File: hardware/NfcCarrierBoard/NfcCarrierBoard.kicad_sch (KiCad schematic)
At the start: 32 parts, among them J1 Barrel_Jack, J2 Conn_01x03, J3 JST SH 4, J4 Grove, J5 Conn_01x03, Q1 NMOS, Q2 NMOS, SW1 RESET

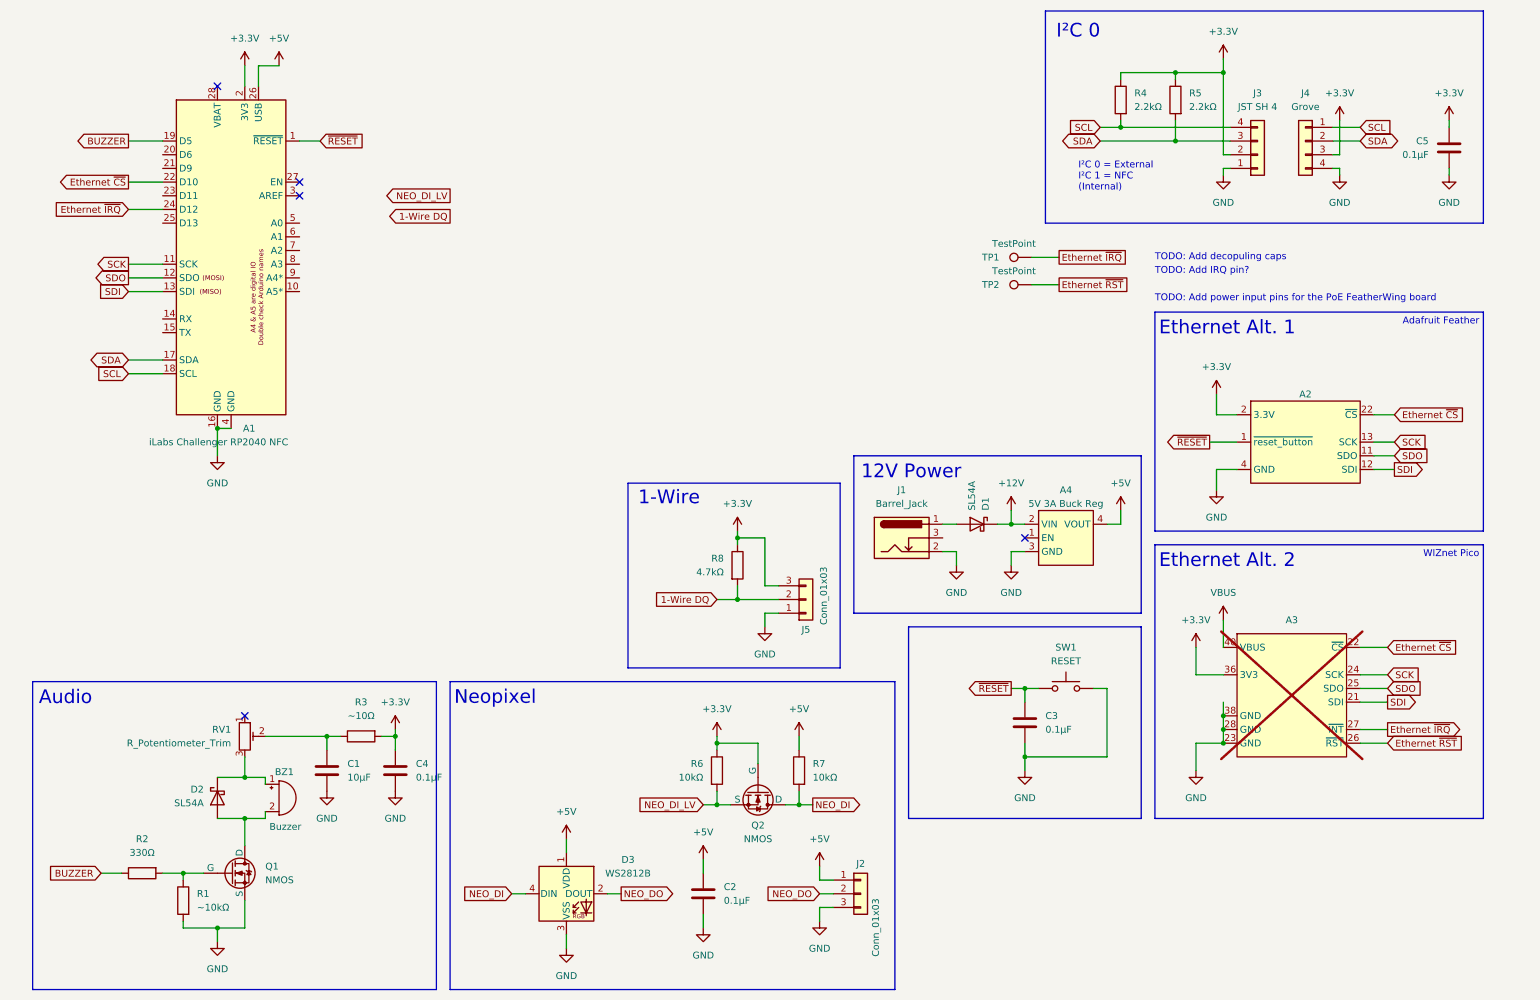
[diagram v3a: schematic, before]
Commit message: Add decopuling caps
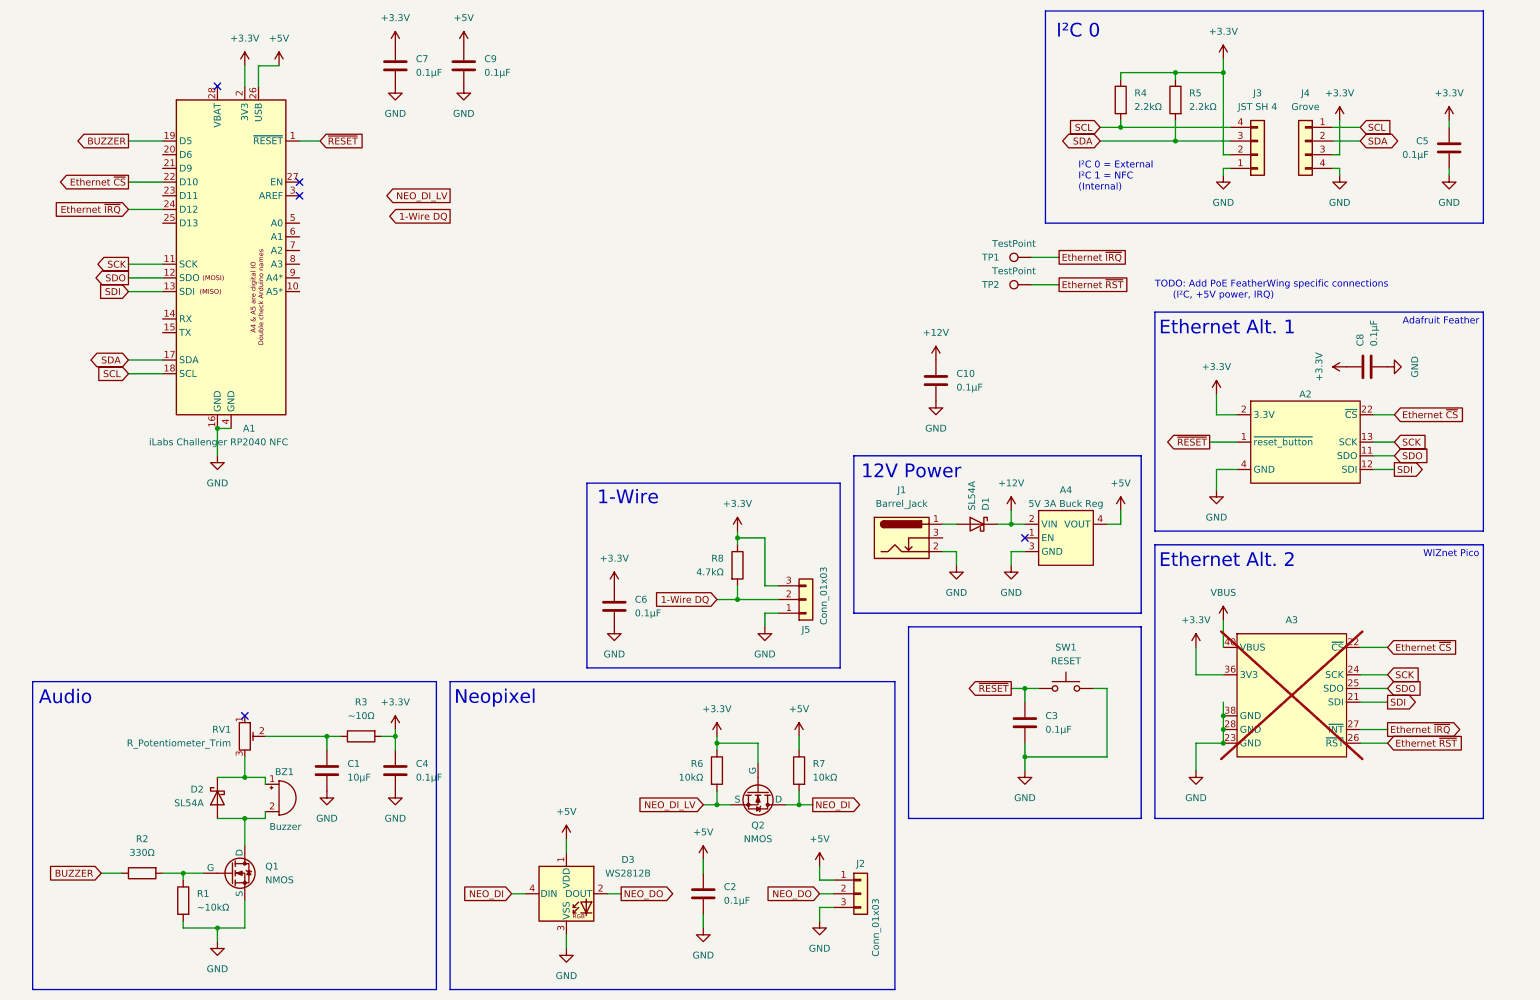
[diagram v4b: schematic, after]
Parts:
- added C10, C6, C7, C8, C9: 0.1µF, Capacitor_SMD:C_0805_2012Metric_Pad1.18x1.45mm_HandSolder, symbol Device:C
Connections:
- net +12V: now also C10.1
- net +3.3V: now also C6.1, C7.1, C8.1
- net +5V: now also C9.1
- net GND: now also C10.2, C6.2, C7.2, C8.2, C9.2
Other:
- note added: "TODO: Add PoE FeatherWing specific connections (I²C, +5V power, IRQ)"
- note removed: "TODO: Add IRQ pin?"
- note removed: "TODO: Add decopuling caps"
- note removed: "TODO: Add power input pins for the PoE FeatherWing board"

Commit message: Add PoE FeatherWing pinouts Add UART headers Fix some ERC errors
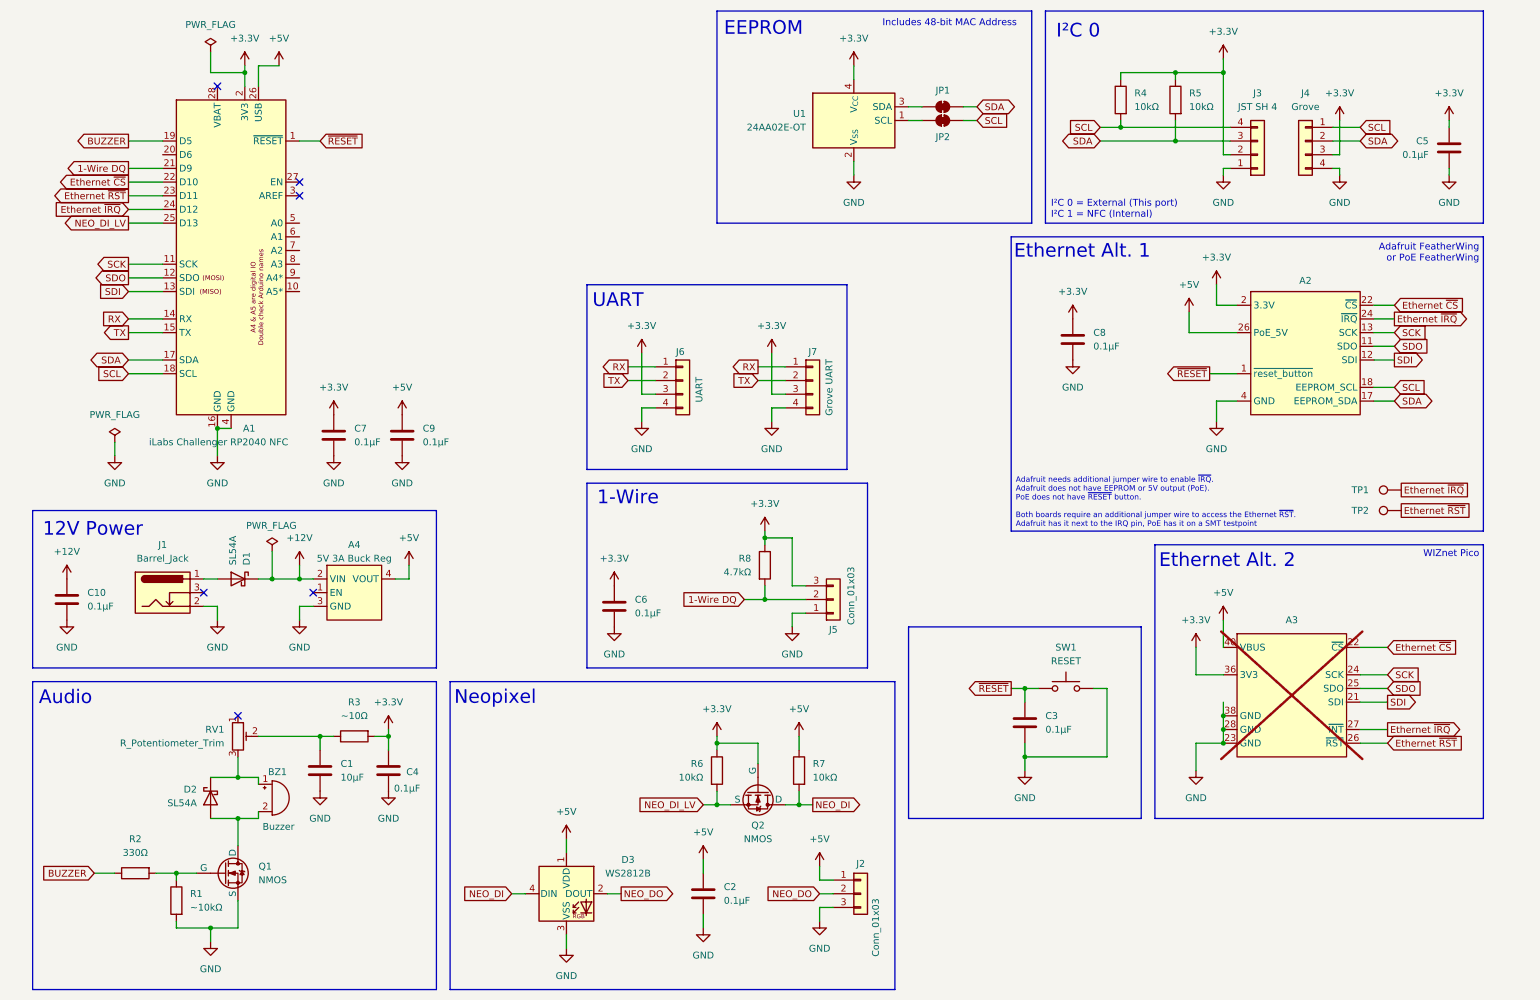
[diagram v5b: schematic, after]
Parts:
- removed A2: ~, Module:Adafruit_Feather, symbol SymbolLibrary:Adafruit_Ethernet_FeatherWing
- added A2: ~, Module:Adafruit_Feather, symbol SymbolLibrary:Silicognition_PoE_FeatherWing
- added J6: UART, symbol Connector_Generic:Conn_01x04
- added J7: Grove UART, Connector:NS-Tech_Grove_1x04_P2mm_Vertical, symbol Connector_Generic:Conn_01x04
- added JP1, JP2: SolderJumper_2_Bridged, Jumper:SolderJumper-2_P1.3mm_Bridged_RoundedPad1.0x1.5mm, symbol Jumper:SolderJumper_2_Bridged
- added U1: 24AA02E-OT, Package_TO_SOT_SMD:SOT-23-5, symbol Memory_EEPROM:24AA02E-OT
- R4, R5: value 2.2kΩ -> 10kΩ
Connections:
- net VBUS is gone; now on net +5V: A3.40 (VBUS)
- net +3.3V: now also A2.2 (3.3V), J6.3 (Pin_3), J7.3 (Pin_3), U1.4 (V_{CC})
- net +5V: now also A2.26 (PoE_5V)
- net 1-Wire DQ: now also A1.21 (D9)
- net Ethernet ~{CS}: now also A2.22 (~{CS})
- net Ethernet ~{IRQ}: now also A2.24 (~{IRQ})
- net Ethernet ~{RST}: now also A1.23 (D11)
- net GND: now also A2.4 (GND), J6.4 (Pin_4), J7.4 (Pin_4), U1.2 (V_{SS})
- net NEO_DI_LV: now also A1.25 (D13)
- net SCK: now also A2.13 (SCK)
- net SCL: now also A2.18 (EEPROM_SCL), JP2.2 (B)
- net SDA: now also A2.17 (EEPROM_SDA), JP1.2 (B)
- net SDI: now also A2.12 (SDI)
- net SDO: now also A2.11 (SDO)
- net ~{RESET}: now also A2.1 (~{reset_button})
- net RX: now reaches A1.14 (RX)
- net RX: now also J6.1 (Pin_1), J7.1 (Pin_1)
- net TX: now reaches A1.15 (TX)
- net TX: now also J6.2 (Pin_2), J7.2 (Pin_2)
- new net: JP2.1 (A), U1.1 (SCL)
- new net: JP1.1 (A), U1.3 (SDA)
- no-connect marks 5 -> 6
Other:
- note added: "Adafruit FeatherWing or PoE FeatherWing"
- note added: "EEPROM"
- note added: "Includes 48-bit MAC Address"
- note added: "UART"
- note removed: "Adafruit Feather"
- note removed: "TODO: Add PoE FeatherWing specific connections (I²C, +5V power, IRQ)"
- moved on the sheet: A4, BZ1, C1, C10, C4, C7, C8, C9, D1, D2, J1, J5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

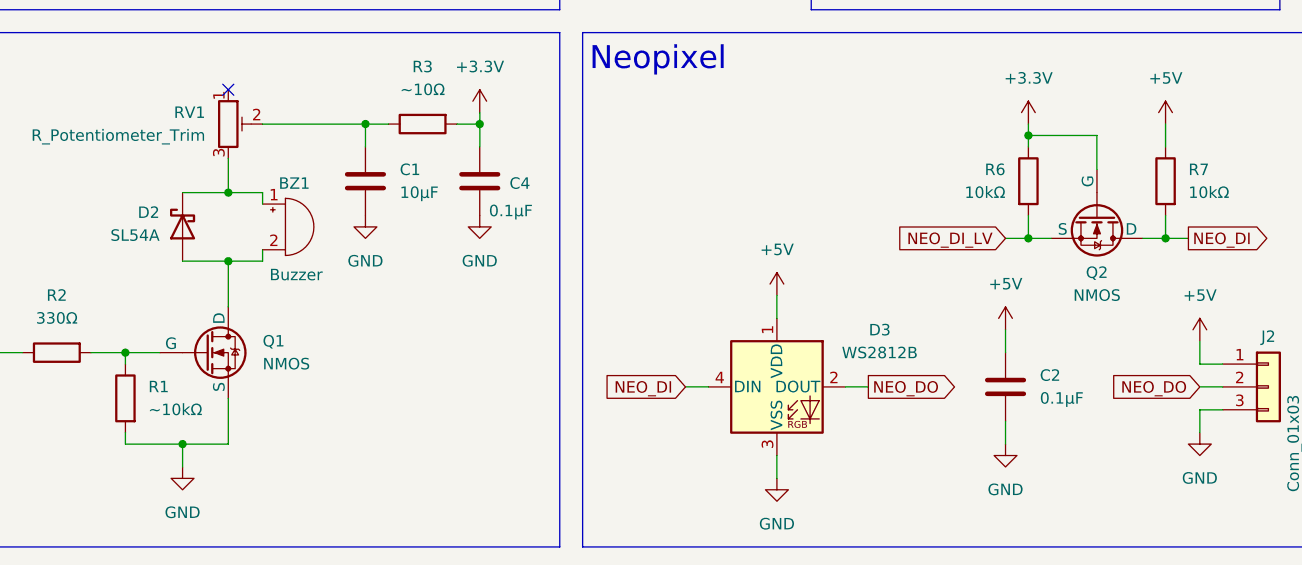
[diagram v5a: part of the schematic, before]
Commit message: Change MOSFET symbols to match pinout of selected parts Add and select more footprints
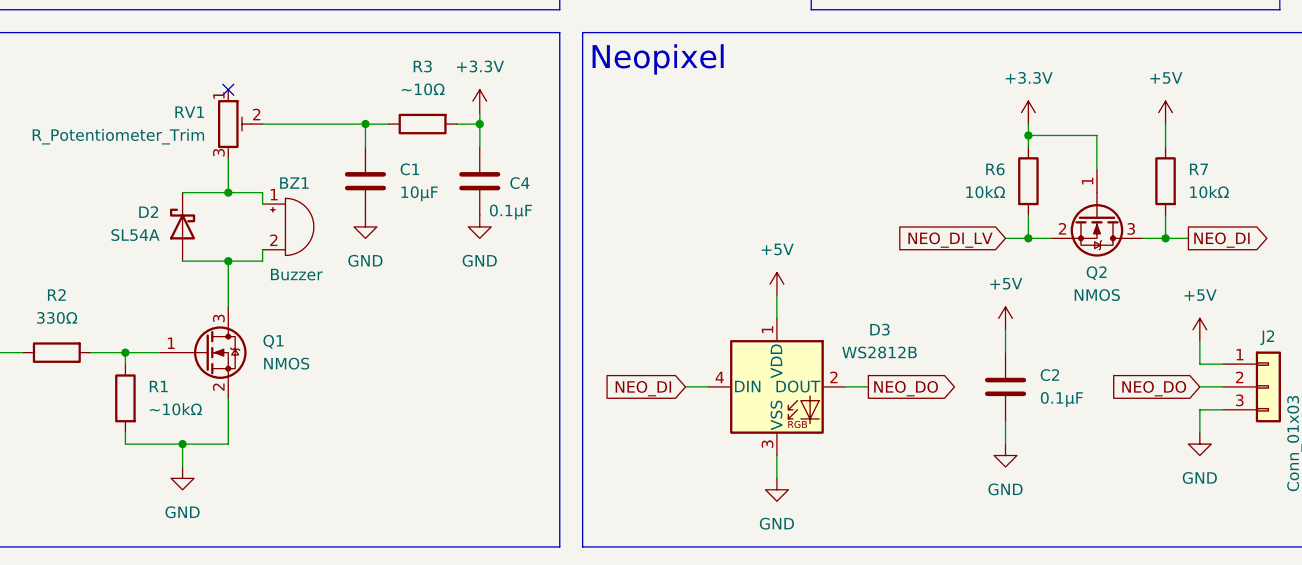
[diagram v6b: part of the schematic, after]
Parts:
- BZ1: footprint (none) -> FootprintLibrary:Buzzer_PUIaudio_AT-1224-TWT_D12_H9_6.5mm
- J3: footprint (none) -> FootprintLibrary:JST-SH-4-top
- J6: footprint (none) -> Connector_PinHeader_2.54mm:PinHeader_1x04_P2.54mm_Vertical
- Q1, Q2: footprint (none) -> Package_TO_SOT_SMD:SOT-323_SC-70_Handsoldering; symbol Simulation_SPICE:NMOS -> Device:Q_NMOS_GSD
- TP1, TP2: footprint (none) -> TestPoint:TestPoint_THTPad_D2.0mm_Drill1.0mm
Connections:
- net +3.3V: now also Q2.1 (G); no longer Q2.2 (G)
- net GND: now also Q1.2 (S); no longer Q1.3 (S)
- net NEO_DI: now also Q2.3 (D); no longer Q2.1 (D)
- net NEO_DI_LV: now also Q2.2 (S); no longer Q2.3 (S)
- net at R1.1, R2.2: now also Q1.1 (G); no longer Q1.2 (G)
- net at BZ1.2 (-), D2.2 (A): now also Q1.3 (D); no longer Q1.1 (D)
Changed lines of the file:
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@@
 			)
 		)
-		(property "Footprint" ""
+		(property "Footprint" "FootprintLibrary:Buzzer_PUIaudio_AT-1224-TWT_D12_H9_6.5mm"
 			(at 57.785 157.48 90)
 			(effects
@@
 			)
 		)
-		(property "Footprint" ""
+		(property "Footprint" "TestPoint:TestPoint_THTPad_D2.0mm_Drill1.0mm"
 			(at 267.97 97.79 0)
 			(effects
@@
 	)
 	(symbol
-		(lib_id "Simulation_SPICE:NMOS")
+		(lib_id "Device:Q_NMOS_GSD")
 		(at 148.59 158.75 270)
 		(unit 1)
@@
 			)
 		)
-		(property "Footprint" ""
+		(property "Footprint" "Package_TO_SOT_SMD:SOT-323_SC-70_Handsoldering"
 			(at 151.13 163.83 0)
 			(effects
@@
 			)
 		)
-		(property "Datasheet" "https://ngspice.sourceforge.io/docs/ngspice-html-manual/manual.xhtml#cha_MOSFETs"
-			(at 135.89 158.75 0)
+		(property "Datasheet" "~"
+			(at 148.59 158.75 0)
 			(effects
 				(font
@@
 			)
 		)
-		(property "Description" "N-MOSFET transistor, drain/source/gate"
+		(property "Description" "N-MOSFET transistor, gate/source/drain"
 			(at 148.59 158.75 0)
 			(effects
@@
 			)
 		)
-		(property "Footprint" ""
+		(property "Footprint" "TestPoint:TestPoint_THTPad_D2.0mm_Drill1.0mm"
 			(at 267.97 101.6 0)
 			(effects
@@
 			)
 		)
-		(property "Footprint" ""
+		(property "Footprint" "FootprintLibrary:JST-SH-4-top"
 			(at 241.3 40.64 0)
 			(effects
@@
 			)
 		)
-		(property "Footprint" ""
+		(property "Footprint" "Connector_PinHeader_2.54mm:PinHeader_1x04_P2.54mm_Vertical"
 			(at 134.62 82.55 0)
 			(effects
@@
 	)
 	(symbol
-		(lib_id "Simulation_SPICE:NMOS")
+		(lib_id "Device:Q_NMOS_GSD")
 		(at 49.53 173.99 0)
 		(unit 1)
@@
 			)
 		)
-		(property "Footprint" ""
+		(property "Footprint" "Package_TO_SOT_SMD:SOT-323_SC-70_Handsoldering"
 			(at 54.61 171.45 0)
 			(effects
@@
 			)
 		)
-		(property "Datasheet" "https://ngspice.sourceforge.io/docs/ngspice-html-manual/manual.xhtml#cha_MOSFETs"
-			(at 49.53 186.69 0)
+		(property "Datasheet" "~"
+			(at 49.53 173.99 0)
 			(effects
 				(font
@@
 			)
 		)
-		(property "Description" "N-MOSFET transistor, drain/source/gate"
+		(property "Description" "N-MOSFET transistor, gate/source/drain"
 			(at 49.53 173.99 0)
 			(effects

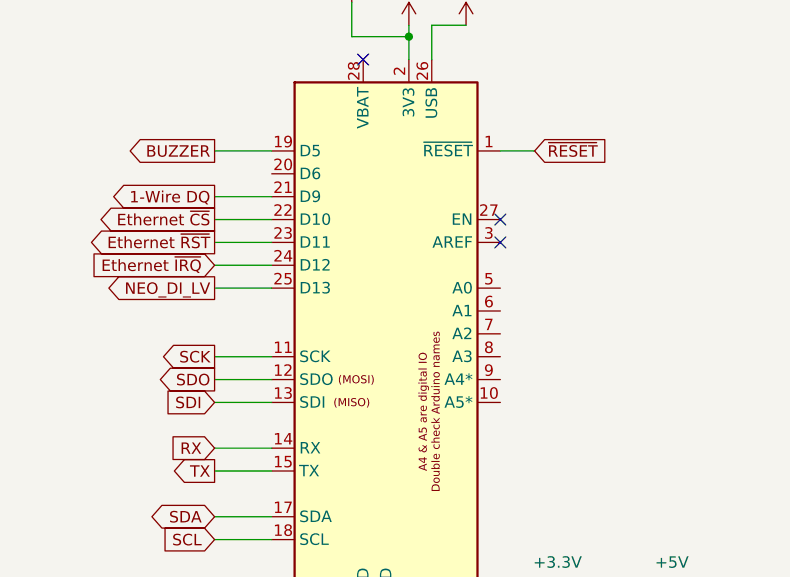
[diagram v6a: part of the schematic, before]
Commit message: Add testpoint pads to unused pins
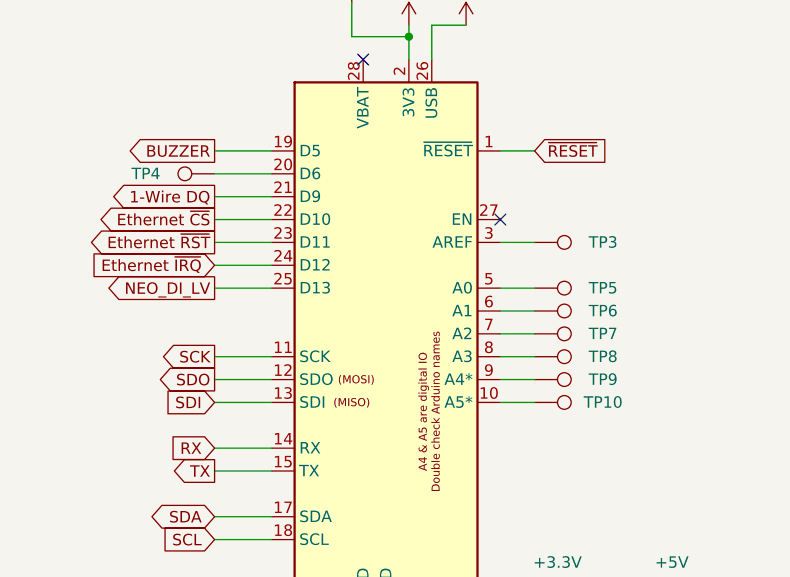
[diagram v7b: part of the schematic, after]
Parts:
- added TP10, TP3, TP4, TP5, TP6, TP7, TP8, TP9: TestPoint, TestPoint:TestPoint_Pad_D2.0mm, symbol Connector:TestPoint
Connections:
- net at A1.10 (A5*): now also TP10.1
- net at A1.20 (D6): now also TP4.1
- net at A1.3 (AREF): now also TP3.1
- net at A1.5 (A0): now also TP5.1
- net at A1.6 (A1): now also TP6.1
- net at A1.7 (A2): now also TP7.1
- net at A1.8 (A3): now also TP8.1
- net at A1.9 (A4*): now also TP9.1
- no-connect marks 6 -> 5
